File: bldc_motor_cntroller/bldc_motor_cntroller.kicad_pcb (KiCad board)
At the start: 2 copper layers, 70 x 50 mm, 141 parts, among them J1 SM06B-SRSS-TB, J10 MR30PW-M 15A (30A), J2 Conn_01x18, J5 0475900001, J6 TC2030 Tag-connect, J7 SH-SM02B-SRSS, J8 XT60, J9 XT60, Q1 CSD18540Q5B, Q2 CSD18540Q5B, Q3 CSD18540Q5B, Q4 CSD18540Q5B, Q5 CSD18540Q5B, Q6 CSD18540Q5B, Q7 CSD18540Q5B, Q8 CSD18540Q5B, SW1 SW_Push, SW2 SW_Push, U1 TCAN332GDCNT, U2 TLV75733PDBV, U3 LM5109BSD, U4 DRV8301DCAR, U5 STM32F405RGTx, Y1 8MHz

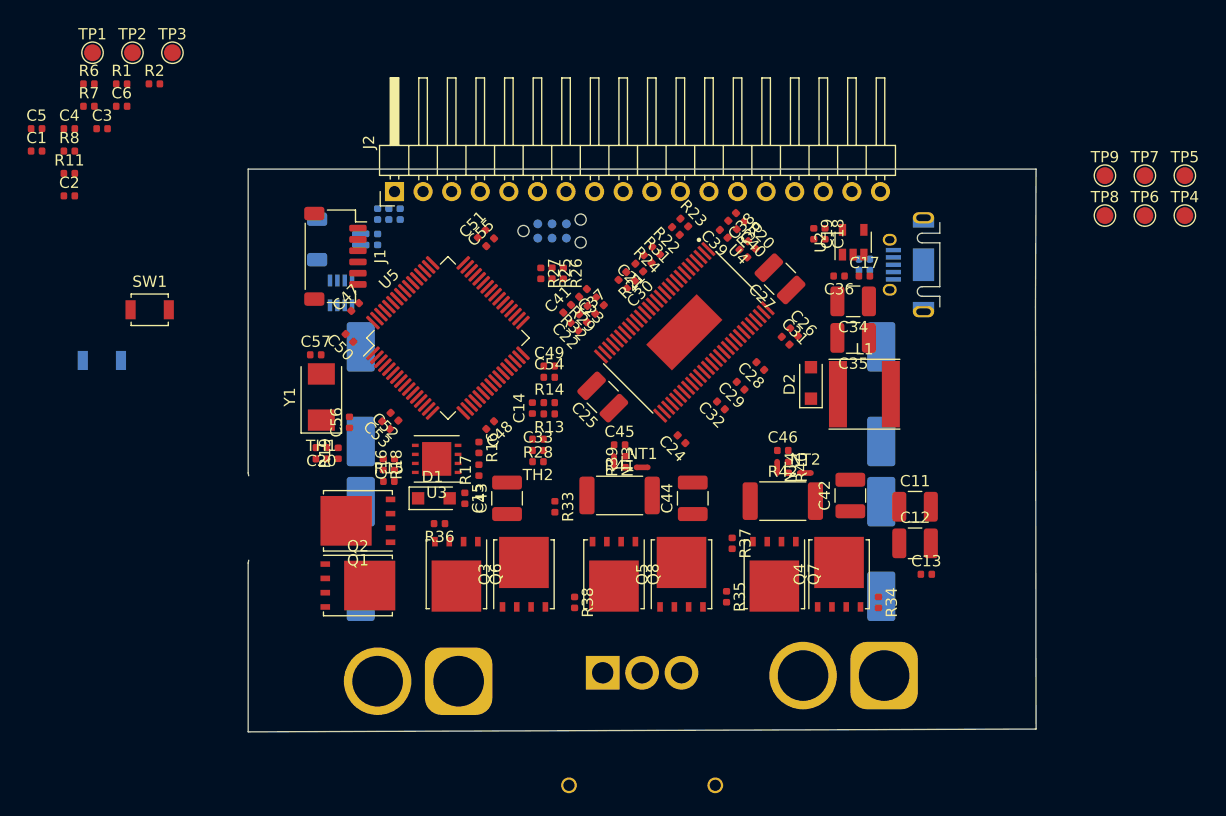
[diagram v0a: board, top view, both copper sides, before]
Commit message: finished placement. reduced pcb size.
Signed-off-by: azmat bilal <azmat.bilal@outlook.com>
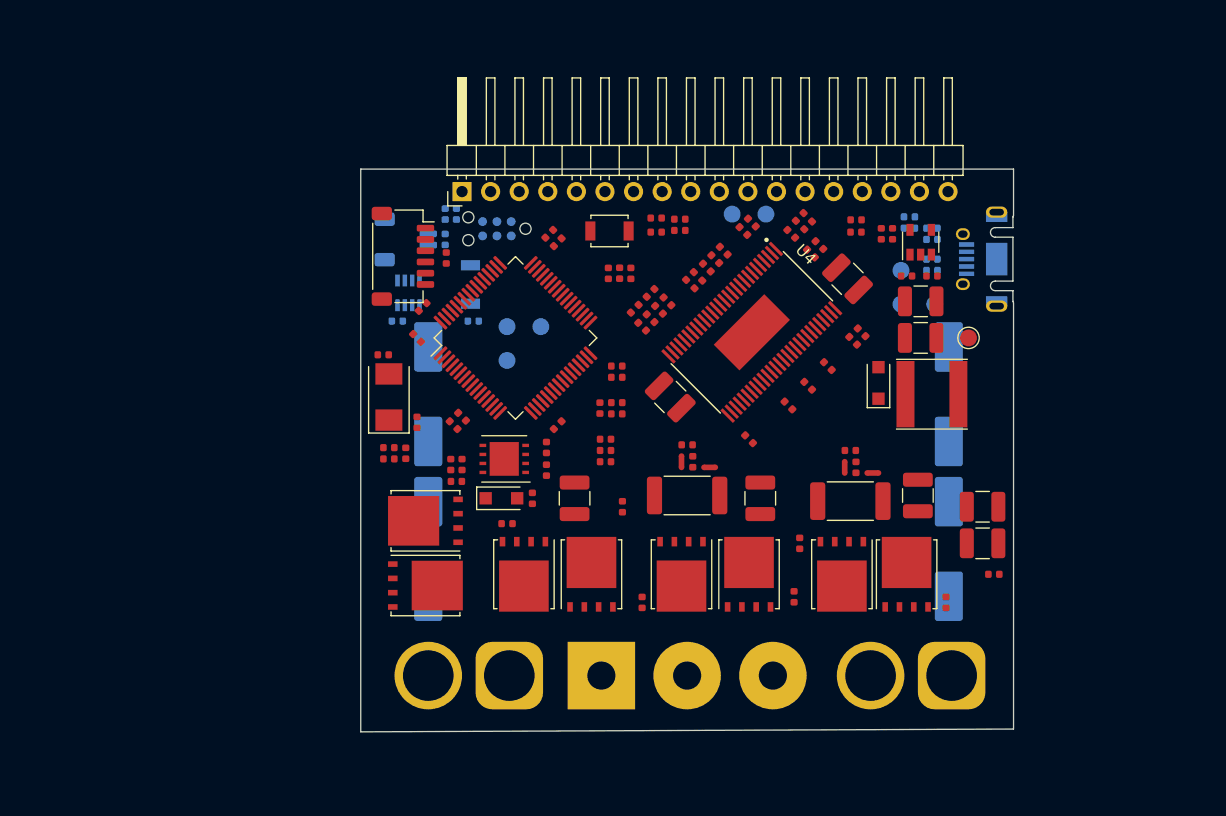
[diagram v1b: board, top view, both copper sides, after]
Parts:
- C3, C5, C6, R11, R6, R8, SW1, TP1, TP2, TP3, TP4, TP5, TP6, TP8, TP9: moved to B.Cu
- J10: footprint Connector_AMASS:AMASS_MR30PW-M_1x03_P3.50mm_Horizontal -> Connector_Wire:SolderWirePad_1x03_P7.62mm_Drill2.5mm
- R5, SW2: moved to F.Cu
- moved C5 80.0 mm to (150.8, 55.2), turned to 180 degrees
- moved TP1 78.1 mm to (151.0, 62.0)
- moved R8 77.0 mm to (150.8, 56.2), turned to 180 degrees
- moved R6 73.9 mm to (148.8, 54.2), turned to 180 degrees
- moved C3 72.3 mm to (148.8, 55.2)
- moved TP2 71.8 mm to (148.0, 62.0)
- moved C4 70.4 mm to (144.0, 54.5)
- moved R7 69.1 mm to (144.0, 55.6)
- moved TP3 67.6 mm to (148.0, 59.0)
- moved TP5 58.8 mm to (116.0, 64.0)
- moved C1 57.6 mm to (128.3, 55.5)
- moved TP9 54.8 mm to (113.0, 64.0)
- moved TP8 54.7 mm to (113.0, 67.0)
- moved C2 52.2 mm to (126.2, 55.6)
- moved R1 51.0 mm to (128.3, 54.5)
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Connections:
- J2 pad 1: /I/O Interface/DEBUG_nRESET -> /I/O Interface/ENC_A
- J2 pad 2: /I/O Interface/DEBUG_SWDIO -> /I/O Interface/ENC_B
- J2 pad 3: /I/O Interface/DEBUG_SWCLK -> /I/O Interface/ENC_Z
- J2 pad 6: /I/O Interface/ENC_A -> /I/O Interface/DEBUG_nRESET
- J2 pad 7: /I/O Interface/ENC_B -> /I/O Interface/DEBUG_SWDIO
- J2 pad 8: /I/O Interface/ENC_Z -> /I/O Interface/DEBUG_SWCLK
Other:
- board size 70 x 50 mm -> 58 x 50 mm

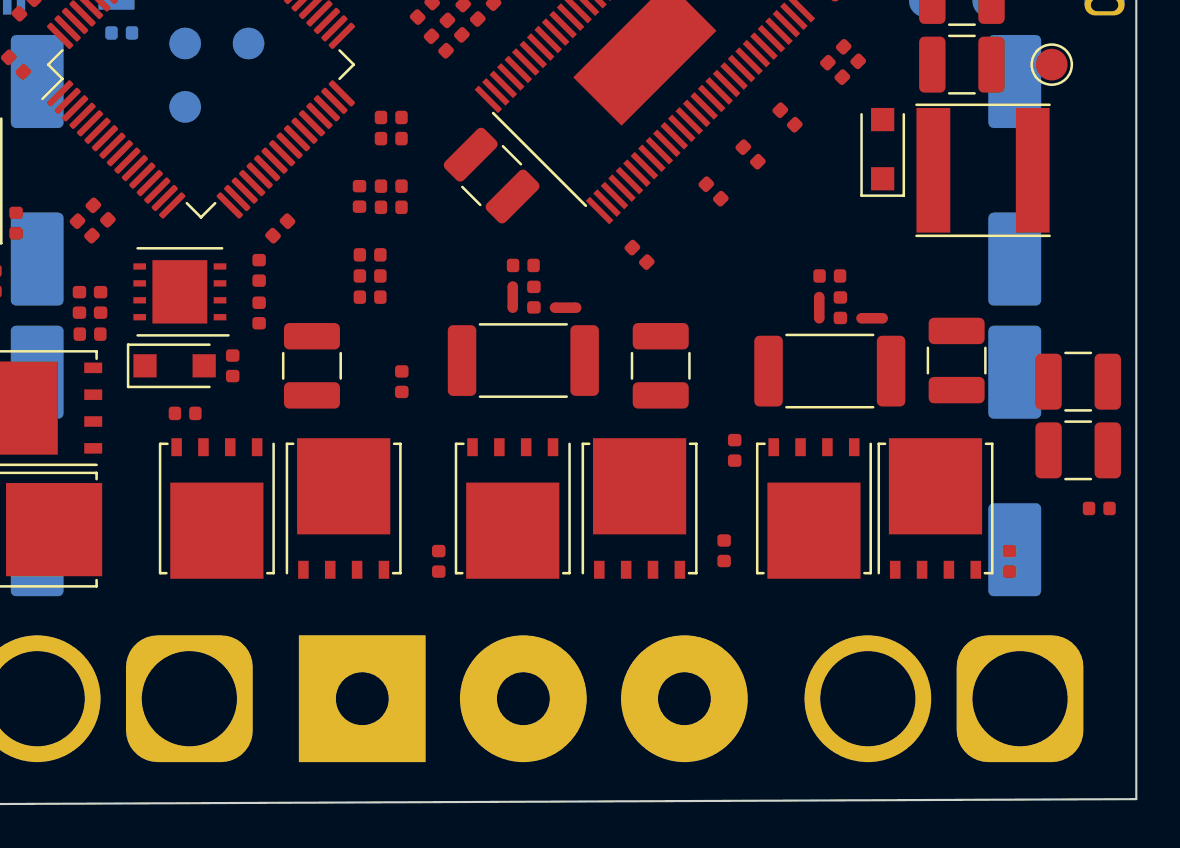
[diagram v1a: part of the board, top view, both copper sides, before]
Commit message: increase layer count to 4. routinng cont. swapped motor outputs.
Signed-off-by: azmat bilal <azmat.bilal@outlook.com>
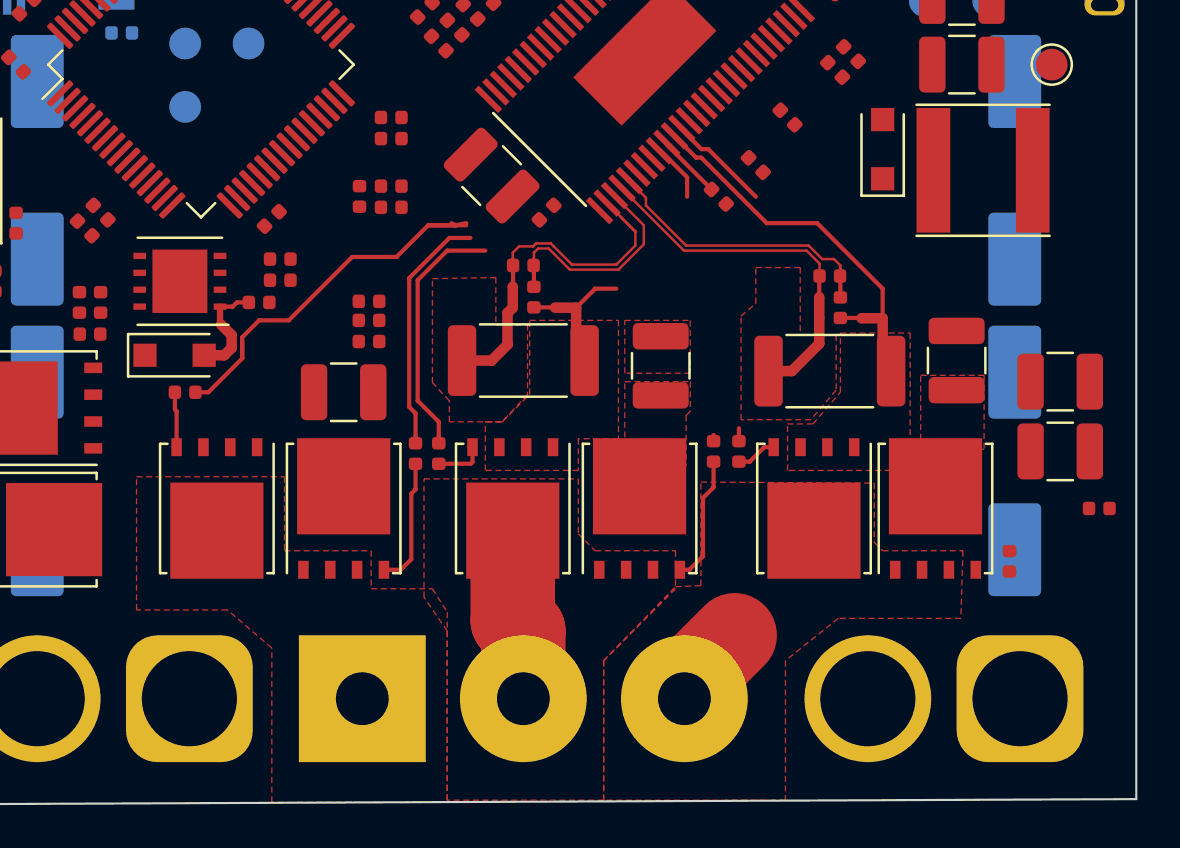
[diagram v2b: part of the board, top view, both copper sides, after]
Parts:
- moved R38 5.10 mm to (125.0, 83.4)
- moved C24 4.83 mm to (130.1, 72.0), turned to 225 degrees
- moved R35 4.73 mm to (138.0, 83.3)
- moved R33 3.46 mm to (123.9, 83.4)
- moved C15 3.25 mm to (116.5, 76.2), turned to 0 degrees
- moved R28 2.20 mm to (121.7, 76.2)
- moved C33 2.10 mm to (121.7, 77.1)
- moved TH2 2.10 mm to (121.7, 78.1)
- moved C43 1.95 mm to (120.5, 80.5), turned to 180 degrees
- moved R17 1.84 mm to (117.5, 75.2), turned to 180 degrees
- moved R16 1.13 mm to (117.5, 74.2), turned to 180 degrees
- moved R36 1.00 mm to (113.0, 80.5)
- moved C12 0.85 mm to (154.4, 83.3)
- moved C11 0.85 mm to (154.4, 80.0)
- moved C48 0.60 mm to (117.1, 72.3)
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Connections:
- J10 pad 2: /Motor Driver/SH_B -> /Motor Driver/SH_C
- J10 pad 3: /Motor Driver/SH_C -> /Motor Driver/SH_B
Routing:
- net /Motor Driver/GL_A: track 0.00 -> 19.5 mm
- net /Motor Driver/SL_B: track 0.00 -> 16.9 mm
- net /Motor Driver/SN1: track 0.00 -> 13.5 mm
- net /Motor Driver/SP1: track 0.00 -> 12.5 mm
- net /Motor Driver/SP2: track 0.00 -> 12.0 mm
- net /Motor Driver/GL_C: track 0.00 -> 11.9 mm
- net /Motor Driver/GH_A: track 0.00 -> 11.6 mm
- net /Motor Driver/SN2: track 0.00 -> 10.7 mm
- net GND: track 0.00 -> 8.45 mm
- net /Motor Driver/SH_C: track 0.00 -> 8.16 mm
- net Net-(Q3-Pad4): track 0.00 -> 6.10 mm
- net Net-(Q5-Pad4): track 0.00 -> 6.04 mm
- net /Motor Driver/GL_B: track 0.00 -> 5.48 mm
- net GVDD: track 0.00 -> 5.07 mm
- net /Motor Driver/SL_C: track 0.00 -> 4.94 mm
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- added copper zone on F.Cu, net /Motor Driver/SH_A
- added copper zone on F.Cu, net /Motor Driver/SH_B
- added copper zone on F.Cu, net /Motor Driver/SH_C
- added copper zone on F.Cu, net /Motor Driver/SL_B
- added copper zone on F.Cu, net /Motor Driver/SL_C
- added copper zone on F.Cu, net GND
- added copper zone on F.Cu, net VDC
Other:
- copper layers 2 -> 4
- net class Default: clearance 0.2 -> 0.12; trace_width 0.25 -> 0.12; via_dia 0.8 -> 0.6; via_drill 0.4 -> 0.25
- net class HV added: clearance 0.3, trace_width 0.12, via_dia 0.6, via_drill 0.25
- rule trace_clearance: 0.2 -> 0.12
- rule trace_min: 0.2 -> 0.1
- rule via_min_drill: 0.3 -> 0.2

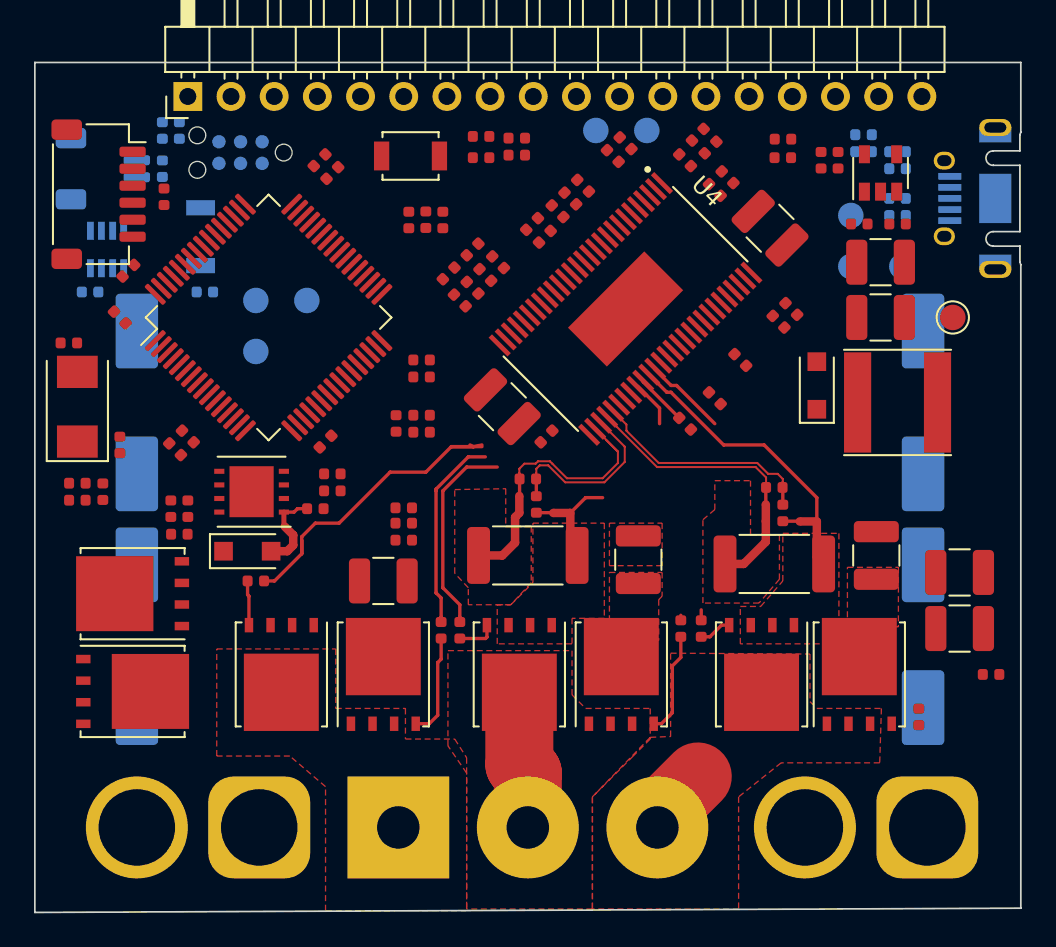
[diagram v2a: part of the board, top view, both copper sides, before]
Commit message: pcb routing cont. swapped 2 motor output pins for better routing.
Signed-off-by: azmat bilal <azmat.bilal@outlook.com>
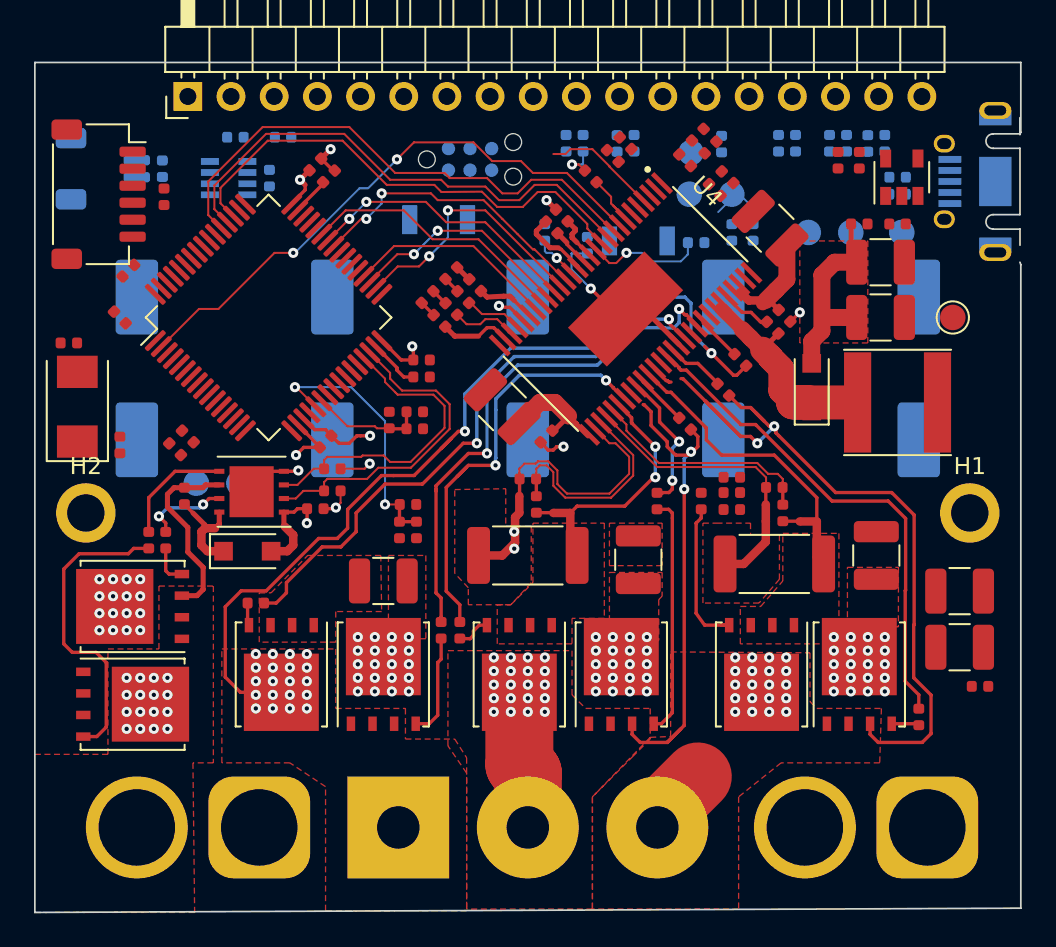
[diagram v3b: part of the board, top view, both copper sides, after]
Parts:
- added C58: 150uF 63V poly, Capacitor_SMD:CP_Elec_10x14.3, B.Cu at (106.0, 68.0)
- added H1: MountingHole_Pad, MountingHole:MountingHole_2.2mm_M2_ISO7380_Pad, F.Cu at (155.0, 76.5)
- added H2: MountingHole_Pad, MountingHole:MountingHole_2.2mm_M2_ISO7380_Pad, F.Cu at (103.0, 76.5)
- C1, C2, C4, R1, R2, R21, R25, R26, R27, R31, R7, SW2: moved to B.Cu
- moved C10 27.9 mm to (129.0, 68.0), turned to 90 degrees
- moved SW1 25.8 mm to (135.5, 60.5), turned to 180 degrees
- moved TP5 23.4 mm to (138.5, 57.8)
- moved R11 22.7 mm to (132.5, 60.8), turned to 90 degrees
- moved TH1 20.0 mm to (122.5, 77.5), turned to 90 degrees
- moved C9 19.7 mm to (140.5, 68.0), turned to 90 degrees
- moved C33 19.4 mm to (141.0, 75.3)
- moved R28 19.4 mm to (141.0, 74.4)
- moved TH2 19.4 mm to (141.0, 76.3)
- moved R25 19.3 mm to (142.2, 60.0)
- moved C20 19.1 mm to (121.5, 77.5), turned to 270 degrees
- moved R27 18.9 mm to (140.4, 54.8), turned to 90 degrees
- moved R19 18.0 mm to (122.0, 76.0), turned to 180 degrees
- moved R26 17.0 mm to (141.0, 60.0)
- moved J6 13.5 mm to (125.6, 55.7), turned to 0 degrees
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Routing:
- net /Motor Driver/SH_A: track 0.00 -> 57.4 mm, vias 0 -> 22
- net /Motor Driver/SH_B: track 3.99 -> 49.5 mm, vias 0 -> 22
- net GND: track 8.45 -> 50.3 mm, vias 0 -> 12
- net /Microcontroller Interface/SPI_M0_nCS: track 0.00 -> 34.0 mm, vias 0 -> 2
- net /Microcontroller Interface/SPI_MOSI: track 0.00 -> 31.5 mm
- net /Microcontroller Interface/SPI_MISO: track 0.00 -> 30.2 mm
- net /Motor Driver/GH_B: track 0.00 -> 29.5 mm
- net /Microcontroller Interface/SPI_SCK: track 0.00 -> 29.0 mm
- net /Motor Driver/SH_C: track 8.16 -> 36.3 mm, vias 0 -> 22
- net /Microcontroller Interface/AUX_H: track 0.00 -> 19.5 mm
- net /Motor Driver/GH_A: track 11.6 -> 30.9 mm, vias 0 -> 2
- net /Microcontroller Interface/AUX_L: track 0.00 -> 18.8 mm
- net Net-(Q2-Pad4): track 0.00 -> 18.6 mm
- net /Microcontroller Interface/M0_AH: track 0.00 -> 17.4 mm, vias 0 -> 2
- net /Microcontroller Interface/M0_BH: track 0.00 -> 16.4 mm, vias 0 -> 2
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- added copper zone on In1.Cu, net GND
- added copper zone on F.Cu, net Net-(C16-Pad2)
- added copper zone on In2.Cu, net VDC
